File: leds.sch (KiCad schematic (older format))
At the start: 34 parts, among them U5 PCA9635PW

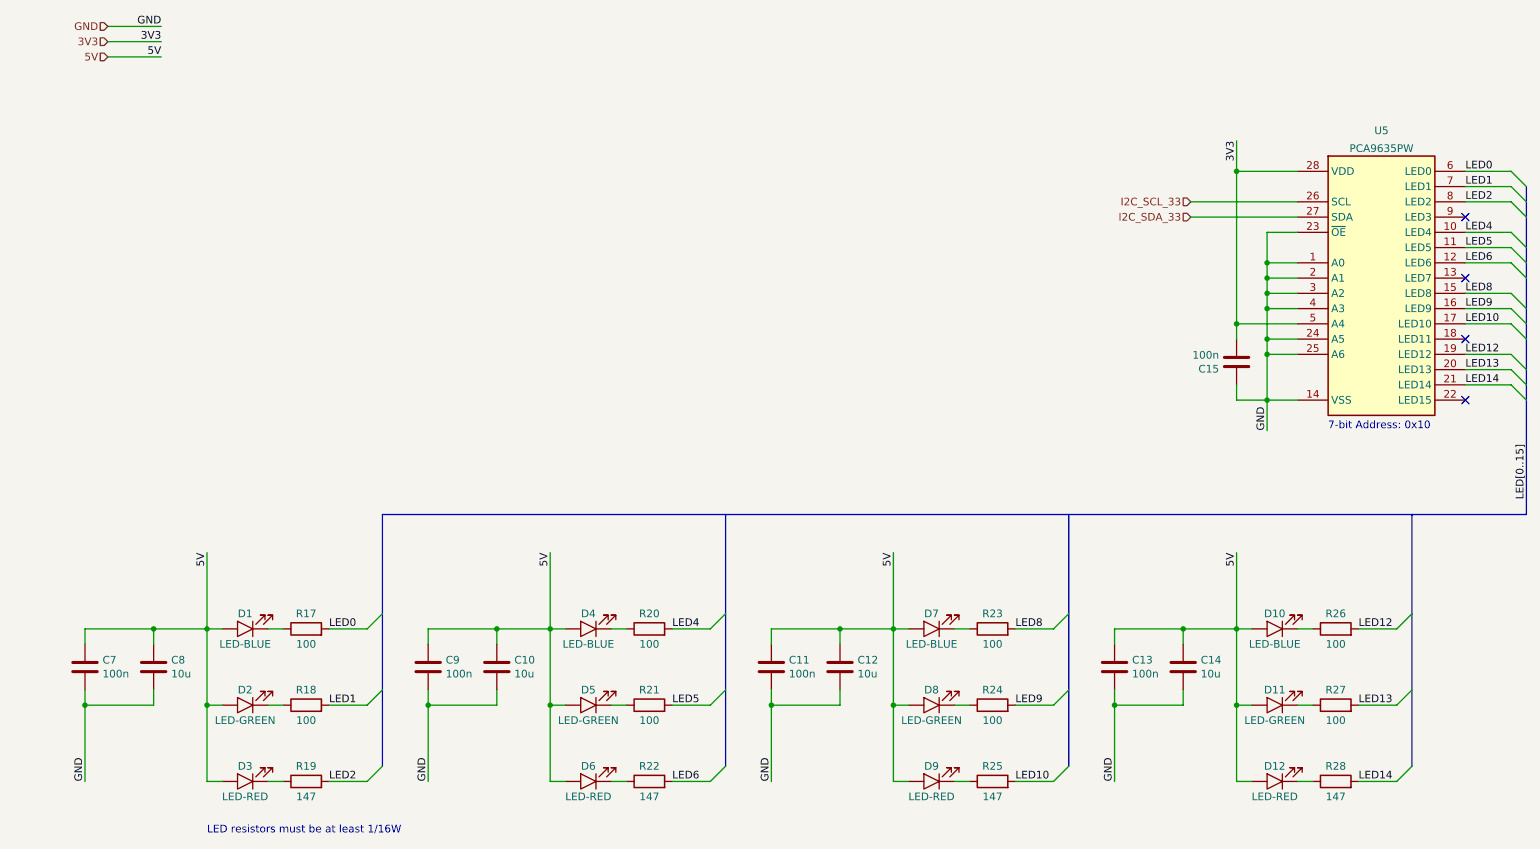
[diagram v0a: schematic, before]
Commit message: Update LED driver to operate at 5V
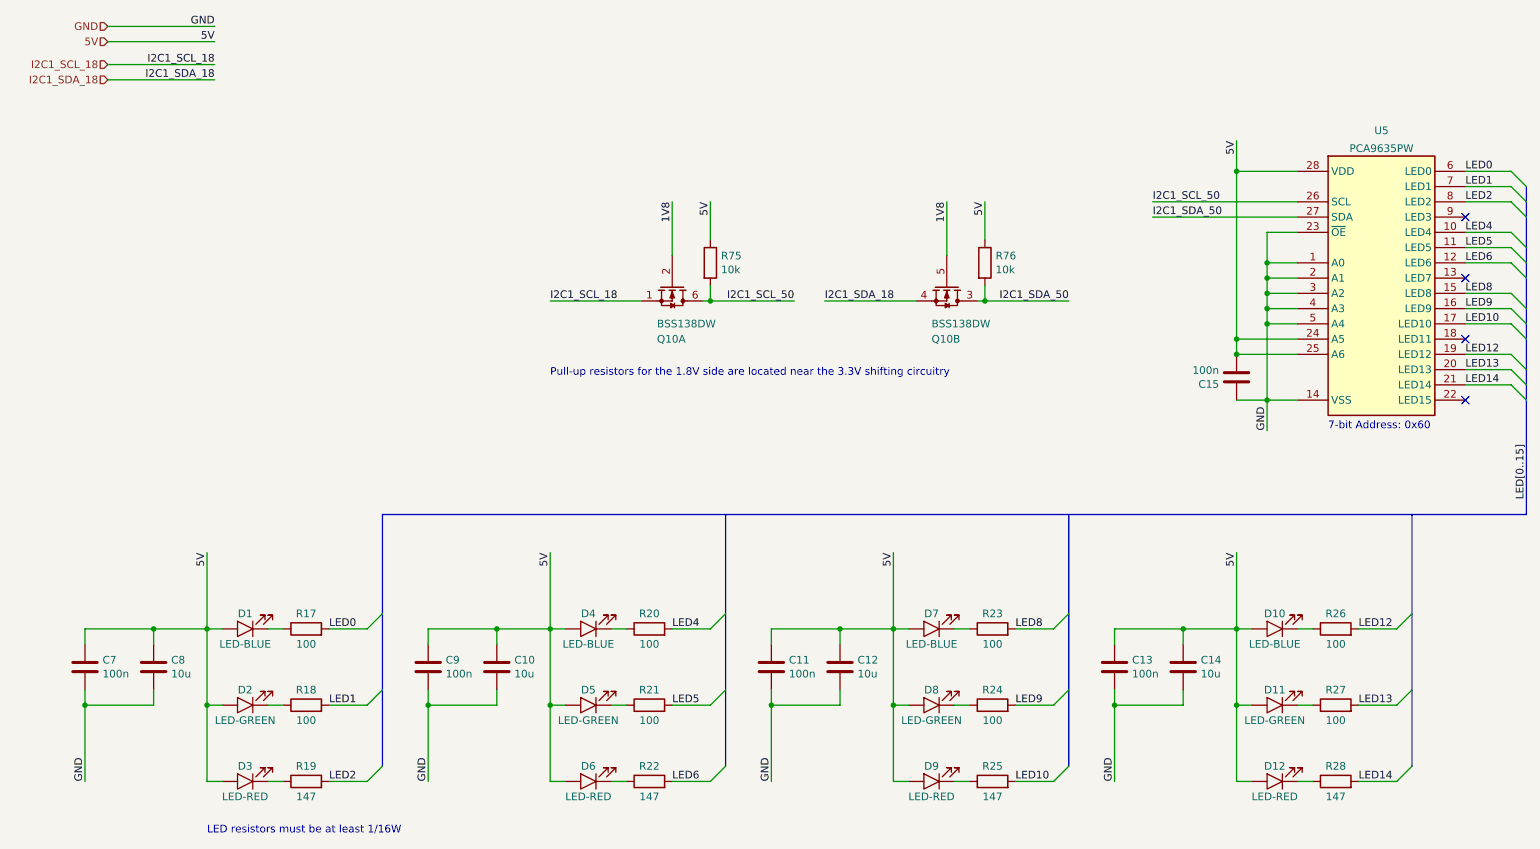
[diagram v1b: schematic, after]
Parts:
- added Q10: BSS138DW, Drone:BSS138DW, symbol Drone:BSS138DW
- added R75, R76: 10k, Drone:R0805, symbol Drone:RES
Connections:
- net 5V: now also C15.2, U5.24 (A5), U5.25 (A6), U5.28 (VDD), R75.1, R76.1
- net GND: now also U5.5 (A4); no longer U5.24 (A5), U5.25 (A6)
- removed net 3V3: C15.2, U5.28 (VDD), U5.5 (A4)
- net I2C_SCL_33 renamed I2C1_SCL_50
- net I2C1_SCL_50: now also Q10.6 (D2), R75.2
- net I2C_SDA_33 renamed I2C1_SDA_50
- net I2C1_SDA_50: now also Q10.3 (D2), R76.2
- new net 1V8: Q10.2 (G2), Q10.5 (G2)
- new net I2C1_SCL_18: Q10.1 (S2)
- new net I2C1_SDA_18: Q10.4 (S2)
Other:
- note added: "7-bit Address: 0x60"
- note added: "Pull-up resistors for the 1.8V side are located near the 3.3V shifting circuitry"
- note removed: "7-bit Address: 0x10"
- moved on the sheet: C15
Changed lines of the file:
@@
 	10400 2000 10500 2100
 Wire Wire Line
-	1200 1250 1550 1250
-Text Label 1550 1250 2    50   ~ 0
+	1200 1150 1900 1150
+Text Label 1900 1150 2    50   ~ 0
 5V
-Text HLabel 1200 1250 0    50   Input ~ 0
+Text HLabel 1200 1150 0    50   Input ~ 0
 5V
 Wire Wire Line
-	1550 1150 1200 1150
-Wire Wire Line
-	1200 1050 1550 1050
-Text Label 1550 1150 2    50   ~ 0
-3V3
-Text Label 1550 1050 2    50   ~ 0
+	1200 1050 1900 1050
+Text Label 1900 1050 2    50   ~ 0
 GND
 Text HLabel 1200 1050 0    50   Input ~ 0
 GND
-Text HLabel 1200 1150 0    50   Input ~ 0
-3V3
 Wire Wire Line
 	8600 1800 8600 2000
@@
 Wire Wire Line
 	8800 2900 8800 2800
-Wire Wire Line
-	9000 3100 8800 3100
-Connection ~ 8800 3100
-Wire Wire Line
-	8800 3100 8800 2900
-Wire Wire Line
-	9000 3200 8800 3200
-Wire Wire Line
-	8800 3200 8800 3100
-Wire Wire Line
-	8600 3000 9000 3000
-Text HLabel 8300 2300 0    50   Input ~ 0
-I2C_SDA_33
-Wire Wire Line
-	8300 2300 9000 2300
-Text HLabel 8300 2200 0    50   Input ~ 0
-I2C_SCL_33
-Wire Wire Line
-	9000 2200 8300 2200
+Text HLabel 1200 1400 0    50   Input ~ 0
+I2C1_SDA_18
+Wire Wire Line
+	1200 1400 1900 1400
+Text HLabel 1200 1300 0    50   Input ~ 0
+I2C1_SCL_18
+Wire Wire Line
+	1900 1300 1200 1300
 Wire Wire Line
 	9000 2400 8800 2400
@@
 Connection ~ 8800 2600
 Wire Wire Line
-	8800 3200 8800 3500
-Wire Wire Line
 	8800 3500 9000 3500
-Connection ~ 8800 3200
 Wire Wire Line
 	8800 3500 8800 3700
@@
 	9000 2000 8600 2000
 Connection ~ 8600 2000
-Wire Wire Line
-	8600 2000 8600 3000
 Text Label 8600 1800 3    50   ~ 0
-3V3
+5V
 Wire Wire Line
 	8600 3500 8800 3500
-Wire Wire Line
-	8600 3500 8600 3400
-Wire Wire Line
-	8600 3100 8600 3000
-Connection ~ 8600 3000
 Text Label 1850 4500 3    50   ~ 0
 5V
@@
 	1050 5500 1050 5400
 Text Notes 9200 3700 0    50   ~ 0
-7-bit Address: 0x10
+7-bit Address: 0x60
 $Comp
 L Drone:LED-RED D3
@@
 L Drone:CAP C?
 U 1 1 5E322DC6
-P 8600 3250
+P 8600 3350
 AR Path="/5E2EDC4D/5E322DC6" Ref="C?"  Part="1"
 AR Path="/5E3090FF/5E322DC6" Ref="C?"  Part="1"
 AR Path="/5E30BD8E/5E322DC6" Ref="C15"  Part="1"
-F 0 "C15" H 8715 3296 50  0000 L CNN
-F 1 "100n" H 8715 3205 50  0000 L CNN
-F 2 "Drone:C0805" H 8638 3100 50  0001 C CNN
-F 3 "~" H 8600 3250 50  0001 C CNN
-	1    8600 3250
+F 0 "C15" H 8715 3396 50  0000 L CNN
+F 1 "100n" H 8715 3305 50  0000 L CNN
+F 2 "Drone:C0805" H 8638 3200 50  0001 C CNN
+F 3 "~" H 8600 3350 50  0001 C CNN
+	1    8600 3350
 	-1   0    0    1
 $EndComp
@@
 NoConn ~ 10100 3100
 NoConn ~ 10100 3500
+Text Label 5150 2200 3    50   ~ 0
+5V
+Wire Wire Line
+	5150 2200 5150 2450
+Wire Wire Line
+	5150 2750 5150 2850
+Wire Wire Line
+	5150 2850 5100 2850
+Text Label 4900 2200 3    50   ~ 0
+1V8
+Wire Wire Line
+	5150 2850 5700 2850
+Connection ~ 5150 2850
+Text Label 4100 2850 0    50   ~ 0
+I2C1_SCL_18
+Text Label 5700 2850 2    50   ~ 0
+I2C1_SCL_50
+Text Label 6950 2200 3    50   ~ 0
+5V
+Wire Wire Line
+	6950 2200 6950 2450
+Wire Wire Line
+	6950 2750 6950 2850
+Wire Wire Line
+	6950 2850 6900 2850
+Text Label 6700 2200 3    50   ~ 0
+1V8
+Wire Wire Line
+	6950 2850 7500 2850
+Connection ~ 6950 2850
+Text Label 5900 2850 0    50   ~ 0
+I2C1_SDA_18
+Text Label 7500 2850 2    50   ~ 0
+I2C1_SDA_50
+$Comp
+L Drone:BSS138DW Q?
+U 1 1 5F011E26
+P 4900 2850
+AR Path="/5E2EDC4D/5F011E26" Ref="Q?"  Part="2"
+AR Path="/5F011E26" Ref="Q?"  Part="2"
+AR Path="/5E30BD8E/5F011E26" Ref="Q10"  Part="1"
+F 0 "Q10" V 5150 2750 50  0000 L CNN
+F 1 "BSS138DW" V 5050 2750 50  0000 L CNN
+F 2 "Drone:BSS138DW" H 5000 2775 50  0001 L CIN
+F 3 "https://www.diodes.com/assets/Datasheets/ds30203.pdf" H 4800 2850 50  0001 L CNN
+	1    4900 2850
+	0    1    1    0
+$EndComp
+$Comp
+L Drone:RES R?
+U 1 1 5F011E32
+P 6950 2600
+AR Path="/5E2EDC4D/5F011E32" Ref="R?"  Part="1"
+AR Path="/5F011E32" Ref="R?"  Part="1"
+AR Path="/5E30BD8E/5F011E32" Ref="R76"  Part="1"
+F 0 "R76" H 7020 2646 50  0000 L CNN
+F 1 "10k" H 7020 2555 50  0000 L CNN
+F 2 "Drone:R0805" V 6880 2600 50  0001 C CNN
+F 3 "~" H 6950 2600 50  0001 C CNN
+	1    6950 2600
+	1    0    0    -1
+$EndComp
+$Comp
+L Drone:RES R?
+U 1 1 5F011E3E
+P 5150 2600
+AR Path="/5E2EDC4D/5F011E3E" Ref="R?"  Part="1"
+AR Path="/5F011E3E" Ref="R?"  Part="1"
+AR Path="/5E30BD8E/5F011E3E" Ref="R75"  Part="1"
+F 0 "R75" H 5220 2646 50  0000 L CNN
+F 1 "10k" H 5220 2555 50  0000 L CNN
+F 2 "Drone:R0805" V 5080 2600 50  0001 C CNN
+F 3 "~" H 5150 2600 50  0001 C CNN
+	1    5150 2600
+	1    0    0    -1
+$EndComp
+$Comp
+L Drone:BSS138DW Q?
+U 2 1 5F011E44
+P 6700 2850
+AR Path="/5E2EDC4D/5F011E44" Ref="Q?"  Part="2"
+AR Path="/5F011E44" Ref="Q?"  Part="1"
+AR Path="/5E30BD8E/5F011E44" Ref="Q10"  Part="2"
+F 0 "Q10" V 6950 2750 50  0000 L CNN
+F 1 "BSS138DW" V 6850 2750 50  0000 L CNN
+F 2 "Drone:BSS138DW" H 6800 2775 50  0001 L CIN
+F 3 "https://www.diodes.com/assets/Datasheets/ds30203.pdf" H 6600 2850 50  0001 L CNN
+	2    6700 2850
+	0    1    1    0
+$EndComp
+Text Label 8050 2300 0    50   ~ 0
+I2C1_SDA_50
+Wire Wire Line
+	8050 2300 9000 2300
+Text Label 8050 2200 0    50   ~ 0
+I2C1_SCL_50
+Wire Wire Line
+	8050 2200 9000 2200
+Text Label 1900 1300 2    50   ~ 0
+I2C1_SCL_18
+Text Label 1900 1400 2    50   ~ 0
+I2C1_SDA_18
+Text Notes 4100 3350 0    50   ~ 0
+Pull-up resistors for the 1.8V side are located near the 3.3V shifting circuitry
+Wire Wire Line
+	6700 2200 6700 2550
+Wire Wire Line
+	5900 2850 6500 2850
+Wire Wire Line
+	4100 2850 4700 2850
+Wire Wire Line
+	4900 2200 4900 2550
+Wire Wire Line
+	8600 2000 8600 3100
+Wire Wire Line
+	8800 2900 8800 3000
 $Comp
 L Drone:PCA9635PW U5
@@
 	1    0    0    -1
 $EndComp
+Wire Wire Line
+	9000 3200 8600 3200
+Connection ~ 8600 3200
+Wire Wire Line
+	9000 3100 8600 3100
+Connection ~ 8600 3100
+Wire Wire Line
+	8600 3100 8600 3200
+Wire Wire Line
+	9000 3000 8800 3000
 Wire Bus Line
 	3000 4250 3000 5900
@@
 Wire Bus Line
 	10500 2100 10500 4250
+Connection ~ 8800 3000
+Wire Wire Line
+	8800 3000 8800 3500
 $EndSCHEMATC

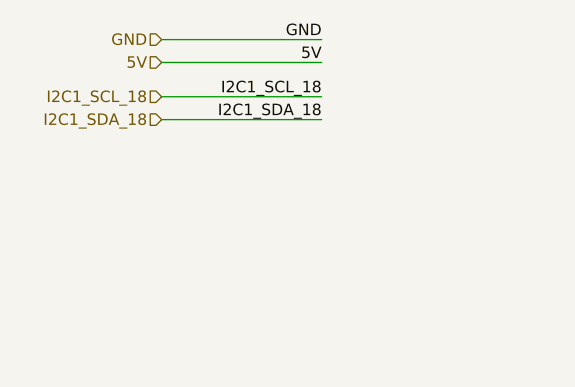
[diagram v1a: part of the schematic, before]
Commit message: Start PCB revision based on testing
1. Split interface schematic into power and interface schematics
2. Remove bi-directional level shifter for UART
3. Connect 1V8 for the LEDs schematic
4. Add new level-shifting buffer and USB hub components
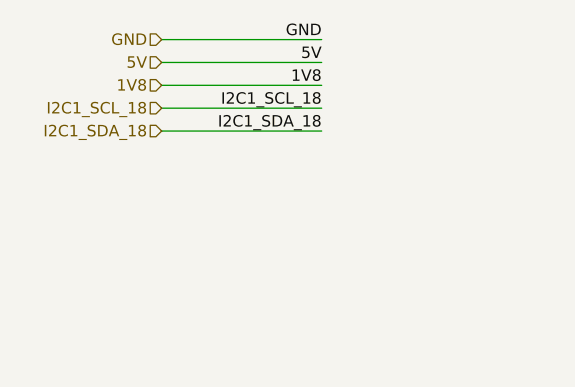
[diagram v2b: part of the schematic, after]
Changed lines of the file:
@@
 $Descr A4 11693 8268
 encoding utf-8
-Sheet 2 6
+Sheet 2 7
 Title ""
 Date ""
@@
 Wire Wire Line
 	8800 2900 8800 2800
-Text HLabel 1200 1400 0    50   Input ~ 0
+Text HLabel 1200 1450 0    50   Input ~ 0
 I2C1_SDA_18
 Wire Wire Line
-	1200 1400 1900 1400
-Text HLabel 1200 1300 0    50   Input ~ 0
+	1200 1450 1900 1450
+Text HLabel 1200 1350 0    50   Input ~ 0
 I2C1_SCL_18
 Wire Wire Line
-	1900 1300 1200 1300
+	1900 1350 1200 1350
 Wire Wire Line
 	9000 2400 8800 2400
@@
 Wire Wire Line
 	8050 2200 9000 2200
-Text Label 1900 1300 2    50   ~ 0
+Text Label 1900 1350 2    50   ~ 0
 I2C1_SCL_18
-Text Label 1900 1400 2    50   ~ 0
+Text Label 1900 1450 2    50   ~ 0
 I2C1_SDA_18
 Text Notes 4100 3350 0    50   ~ 0
@@
 Wire Wire Line
 	9000 3000 8800 3000
+Connection ~ 8800 3000
+Wire Wire Line
+	8800 3000 8800 3500
+Wire Wire Line
+	1200 1250 1900 1250
+Text Label 1900 1250 2    50   ~ 0
+1V8
+Text HLabel 1200 1250 0    50   Input ~ 0
+1V8
 Wire Bus Line
 	3000 4250 3000 5900
@@
 Wire Bus Line
 	10500 2100 10500 4250
-Connection ~ 8800 3000
-Wire Wire Line
-	8800 3000 8800 3500
 $EndSCHEMATC

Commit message: Route remaining connections. Check schematics for errors.
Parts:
- added C47, C70: 100n, Drone:C0805, symbol Drone:CAP
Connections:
- net 5V: now also C47.2, C70.2
- net GND: now also C47.1, C70.1
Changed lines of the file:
@@
 Text HLabel 1200 1250 0    50   Input ~ 0
 1V8
+Wire Wire Line
+	5700 2550 5700 2700
+Text Label 5700 2700 1    50   ~ 0
+GND
+$Comp
+L Drone:CAP C?
+U 1 1 60C0209F
+P 5700 2400
+AR Path="/5E2EDC4D/60C0209F" Ref="C?"  Part="1"
+AR Path="/5E3090FF/60C0209F" Ref="C?"  Part="1"
+AR Path="/5E30BD8E/60C0209F" Ref="C47"  Part="1"
+F 0 "C47" H 5815 2446 50  0000 L CNN
+F 1 "100n" H 5815 2355 50  0000 L CNN
+F 2 "Drone:C0805" H 5738 2250 50  0001 C CNN
+F 3 "~" H 5700 2400 50  0001 C CNN
+	1    5700 2400
+	1    0    0    1
+$EndComp
+Wire Wire Line
+	5150 2200 5700 2200
+Wire Wire Line
+	5700 2200 5700 2250
+Wire Wire Line
+	7500 2550 7500 2700
+Text Label 7500 2700 1    50   ~ 0
+GND
+$Comp
+L Drone:CAP C?
+U 1 1 60C4C34E
+P 7500 2400
+AR Path="/5E2EDC4D/60C4C34E" Ref="C?"  Part="1"
+AR Path="/5E3090FF/60C4C34E" Ref="C?"  Part="1"
+AR Path="/5E30BD8E/60C4C34E" Ref="C70"  Part="1"
+F 0 "C70" H 7615 2446 50  0000 L CNN
+F 1 "100n" H 7615 2355 50  0000 L CNN
+F 2 "Drone:C0805" H 7538 2250 50  0001 C CNN
+F 3 "~" H 7500 2400 50  0001 C CNN
+	1    7500 2400
+	1    0    0    1
+$EndComp
+Wire Wire Line
+	6950 2200 7500 2200
+Wire Wire Line
+	7500 2200 7500 2250
 Wire Bus Line
 	3000 4250 3000 5900
